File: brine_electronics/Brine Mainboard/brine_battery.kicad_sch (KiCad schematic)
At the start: 2 parts, among them J1 Conn_01x02_Socket

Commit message: Updated electronics/enclosure designs
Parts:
- BATT1: now left out of the parts list
- J1: footprint Connector_JST:JST_PH_B2B-PH-K_1x02_P2.00mm_Vertical -> Connector_JST:JST_PH_S2B-PH-K_1x02_P2.00mm_Horizontal
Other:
- moved on the sheet: BATT1
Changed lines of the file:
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@@
 	(wire
 		(pts
-			(xy 139.7 113.03) (xy 163.83 113.03)
-		)
-		(stroke
-			(width 0)
-			(type default)
-		)
-	)
-	(wire
-		(pts
-			(xy 139.7 115.57) (xy 163.83 115.57)
+			(xy 139.7 100.33) (xy 163.83 100.33)
+		)
+		(stroke
+			(width 0)
+			(type default)
+		)
+	)
+	(wire
+		(pts
+			(xy 139.7 102.87) (xy 163.83 102.87)
 		)
 		(stroke
@@
 	(hierarchical_label "BATT"
 		(shape output)
-		(at 163.83 113.03 0)
+		(at 163.83 100.33 0)
 		(effects
 			(font
@@
 	(symbol
 		(lib_id "power:GND")
-		(at 163.83 115.57 90)
+		(at 163.83 102.87 90)
 		(unit 1)
 		(exclude_from_sim no)
@@
 		(fields_autoplaced yes)
 		(property "Reference" "#PWR08"
-			(at 170.18 115.57 0)
+			(at 170.18 102.87 0)
 			(effects
 				(font
@@
 		)
 		(property "Value" "GND"
-			(at 167.64 115.5699 90)
+			(at 167.64 102.8699 90)
 			(effects
 				(font
@@
 		)
 		(property "Footprint" ""
-			(at 163.83 115.57 0)
+			(at 163.83 102.87 0)
 			(effects
 				(font
@@
 		)
 		(property "Datasheet" ""
-			(at 163.83 115.57 0)
+			(at 163.83 102.87 0)
 			(effects
 				(font
@@
 		)
 		(property "Description" "Power symbol creates a global label with name \"GND\" , ground"
-			(at 163.83 115.57 0)
+			(at 163.83 102.87 0)
 			(effects
 				(font
@@
 			)
 		)
-		(property "Footprint" "Connector_JST:JST_PH_B2B-PH-K_1x02_P2.00mm_Vertical"
+		(property "Footprint" "Connector_JST:JST_PH_S2B-PH-K_1x02_P2.00mm_Horizontal"
 			(at 134.62 90.17 0)
 			(effects
@@
 	(symbol
 		(lib_id "Connector:Conn_01x02_Pin")
-		(at 134.62 113.03 0)
-		(unit 1)
-		(exclude_from_sim no)
-		(in_bom yes)
+		(at 134.62 100.33 0)
+		(unit 1)
+		(exclude_from_sim no)
+		(in_bom no)
 		(on_board yes)
 		(dnp yes)
 		(property "Reference" "BATT1"
-			(at 130.556 114.3 0)
+			(at 130.556 101.6 0)
 			(effects
 				(font
@@
 		)
 		(property "Value" "Conn_01x02_Pin"
-			(at 135.255 110.49 0)
+			(at 135.255 97.79 0)
 			(effects
 				(font
@@
 		)
 		(property "Footprint" "Connector_PinHeader_2.54mm:PinHeader_1x02_P2.54mm_Vertical"
-			(at 134.62 113.03 0)
+			(at 134.62 100.33 0)
 			(effects
 				(font
@@
 		)
 		(property "Datasheet" "~"
-			(at 134.62 113.03 0)
+			(at 134.62 100.33 0)
 			(effects
 				(font
@@
 		)
 		(property "Description" "Generic connector, single row, 01x02, script generated"
-			(at 134.62 113.03 0)
-			(effects
-				(font
+			(at 134.62 100.33 0)
+			(effects
+				(font

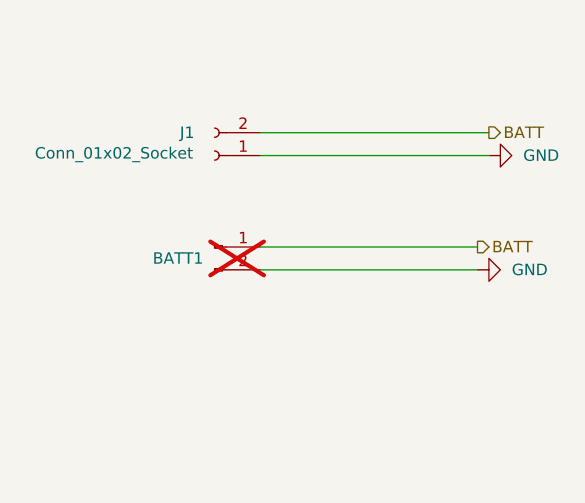
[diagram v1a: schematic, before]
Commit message: Implemented power latch circuit ⚡
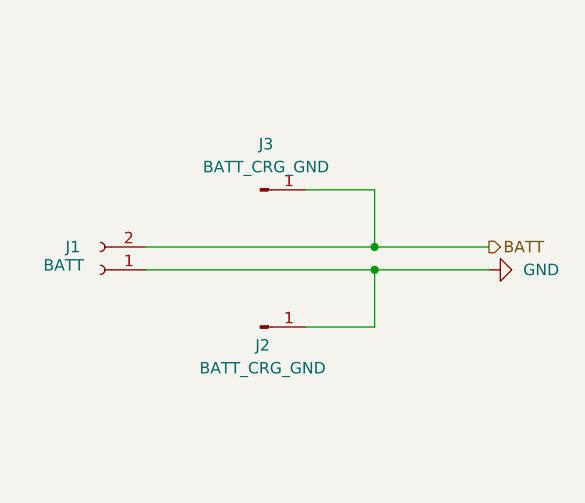
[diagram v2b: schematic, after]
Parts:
- removed BATT1: Conn_01x02_Pin, Connector_PinHeader_2.54mm:PinHeader_1x02_P2.54mm_Vertical, symbol Connector:Conn_01x02_Pin
- added J2, J3: BATT_CRG_GND, Connector_Wire:SolderWirePad_1x01_SMD_1.5x3mm, symbol Connector:Conn_01x01_Pin
- J1: value Conn_01x02_Socket -> BATT
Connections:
- net BATT: now also J3.1 (Pin_1)
- net GND: now also J2.1 (Pin_1)
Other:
- moved on the sheet: J1

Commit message: Resolved schematic DRC issues ✅
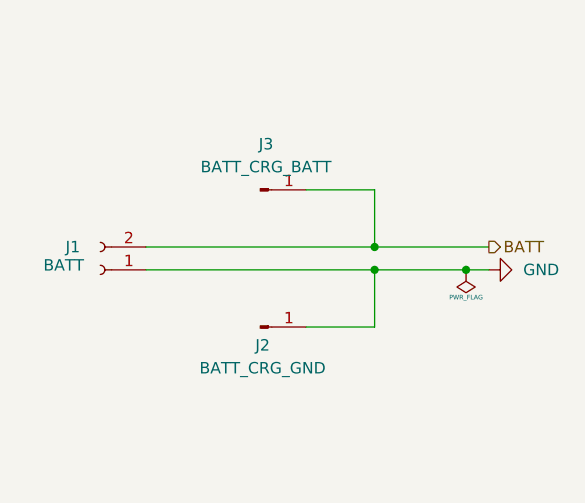
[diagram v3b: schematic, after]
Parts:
- J3: value BATT_CRG_GND -> BATT_CRG_BATT
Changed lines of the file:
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@@
 	(title_block
 		(title "Brine - Battery")
-		(date "2026-04-03")
+		(date "2026-04-07")
 		(rev "1.0.0")
 		(company "Splendid Endeavors")
@@
 		(color 0 0 0 0)
 	)
+	(junction
+		(at 162.56 102.87)
+		(diameter 0)
+		(color 0 0 0 0)
+	)
 	(wire
 		(pts
@@
 	(wire
 		(pts
-			(xy 152.4 102.87) (xy 165.1 102.87)
+			(xy 152.4 102.87) (xy 162.56 102.87)
 		)
 		(stroke
@@
 		(pts
 			(xy 144.78 93.98) (xy 152.4 93.98)
+		)
+		(stroke
+			(width 0)
+			(type default)
+		)
+	)
+	(wire
+		(pts
+			(xy 162.56 102.87) (xy 165.1 102.87)
 		)
 		(stroke
@@
 			)
 		)
-		(property "Value" "BATT_CRG_GND"
+		(property "Value" "BATT_CRG_BATT"
 			(at 140.335 91.44 0)
 			(effects
@@
 					(unit 1)
 				)
+			)
+		)
+	)
+	(symbol
+		(lib_id "power:PWR_FLAG")
+		(at 162.56 102.87 180)
+		(unit 1)
+		(exclude_from_sim no)
+		(in_bom yes)
+		(on_board yes)
+		(dnp no)
+		(property "Reference" "#FLG03"
+			(at 162.56 104.775 0)
+			(effects
+				(font
+					(size 1.27 1.27)
+				)
+				(hide yes)
+			)
+		)
+		(property "Value" "PWR_FLAG"
+			(at 162.56 105.918 0)
+			(effects
+				(font
+					(size 0.508 0.508)
+				)
+			)
+		)
+		(property "Footprint" ""
+			(at 162.56 102.87 0)
+			(effects
+				(font
+					(size 1.27 1.27)
+				)
+				(hide yes)
+			)
+		)
+		(property "Datasheet" "~"
+			(at 162.56 102.87 0)
+			(effects
+				(font
+					(size 1.27 1.27)
+				)
+				(hide yes)
+			)
+		)
+		(property "Description" "Special symbol for telling ERC where power comes from"
+			(at 162.56 102.87 0)
+			(effects
+				(font
+					(size 1.27 1.27)
+				)
+				(hide yes)
+			)
+		)
+		(pin "1"
+		)
+		(instances
+			(project ""
+				(path "/da3a4ef2-0e38-46f1-a1fc-55d8e0a83a54/cb6fa39a-9a0c-434c-b5c9-65b8cf34a8e9"
+					(reference "#FLG03")
+					(unit 1)
+				)

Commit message: Updated lower latch circuit ⚡
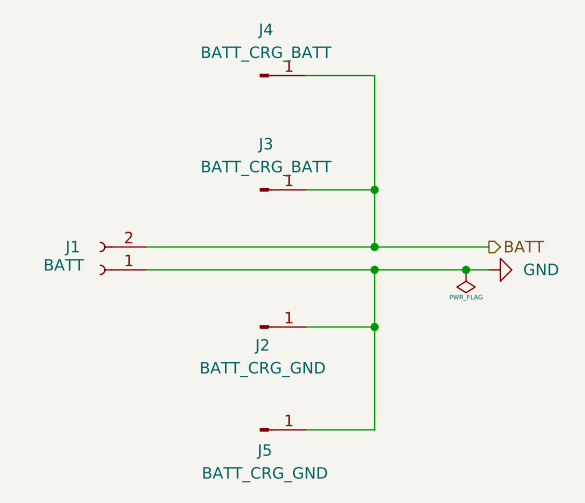
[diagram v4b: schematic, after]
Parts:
- added J4: BATT_CRG_BATT, Connector_PinHeader_1.00mm:PinHeader_1x01_P1.00mm_Vertical, symbol Connector:Conn_01x01_Pin
- added J5: BATT_CRG_GND, Connector_PinHeader_1.00mm:PinHeader_1x01_P1.00mm_Vertical, symbol Connector:Conn_01x01_Pin
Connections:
- net BATT: now also J4.1 (Pin_1)
- net GND: now also J5.1 (Pin_1)

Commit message: Updated production files 🏭
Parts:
- J1, J2, J3, J4, J5: now left out of the parts list
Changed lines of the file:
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@@
 		(body_style 1)
 		(exclude_from_sim no)
-		(in_bom yes)
+		(in_bom no)
 		(on_board yes)
 		(in_pos_files yes)
@@
 		)
 		(property "Description" "Generic connector, single row, 01x02, script generated"
+			(at 121.92 102.87 0)
+			(hide yes)
+			(show_name no)
+			(do_not_autoplace no)
+			(effects
+				(font
+					(size 1.27 1.27)
+				)
+			)
+		)
+		(property "Color" ""
+			(at 121.92 102.87 0)
+			(hide yes)
+			(show_name no)
+			(do_not_autoplace no)
+			(effects
+				(font
+					(size 1.27 1.27)
+				)
+			)
+		)
+		(property "LCSC Part #" ""
 			(at 121.92 102.87 0)
 			(hide yes)
@@
 		(body_style 1)
 		(exclude_from_sim no)
-		(in_bom yes)
+		(in_bom no)
 		(on_board yes)
 		(in_pos_files yes)
@@
 		)
 		(property "Description" "Generic connector, single row, 01x01, script generated"
+			(at 139.7 120.65 0)
+			(hide yes)
+			(show_name no)
+			(do_not_autoplace no)
+			(effects
+				(font
+					(size 1.27 1.27)
+				)
+			)
+		)
+		(property "Color" ""
+			(at 139.7 120.65 0)
+			(hide yes)
+			(show_name no)
+			(do_not_autoplace no)
+			(effects
+				(font
+					(size 1.27 1.27)
+				)
+			)
+		)
+		(property "LCSC Part #" ""
 			(at 139.7 120.65 0)
 			(hide yes)
@@
 		(body_style 1)
 		(exclude_from_sim no)
-		(in_bom yes)
+		(in_bom no)
 		(on_board yes)
 		(in_pos_files yes)
@@
 		)
 		(property "Description" "Generic connector, single row, 01x01, script generated"
+			(at 139.7 93.98 0)
+			(hide yes)
+			(show_name no)
+			(do_not_autoplace no)
+			(effects
+				(font
+					(size 1.27 1.27)
+				)
+			)
+		)
+		(property "Color" ""
+			(at 139.7 93.98 0)
+			(hide yes)
+			(show_name no)
+			(do_not_autoplace no)
+			(effects
+				(font
+					(size 1.27 1.27)
+				)
+			)
+		)
+		(property "LCSC Part #" ""
 			(at 139.7 93.98 0)
 			(hide yes)
@@
 		(body_style 1)
 		(exclude_from_sim no)
-		(in_bom yes)
+		(in_bom no)
 		(on_board yes)
 		(in_pos_files yes)
@@
 		)
 		(property "Description" "Generic connector, single row, 01x01, script generated"
+			(at 139.7 109.22 0)
+			(hide yes)
+			(show_name no)
+			(do_not_autoplace no)
+			(effects
+				(font
+					(size 1.27 1.27)
+				)
+			)
+		)
+		(property "Color" ""
+			(at 139.7 109.22 0)
+			(hide yes)
+			(show_name no)
+			(do_not_autoplace no)
+			(effects
+				(font
+					(size 1.27 1.27)
+				)
+			)
+		)
+		(property "LCSC Part #" ""
 			(at 139.7 109.22 0)
 			(hide yes)
@@
 		(body_style 1)
 		(exclude_from_sim no)
-		(in_bom yes)
+		(in_bom no)
 		(on_board yes)
 		(in_pos_files yes)
@@
 			(at 139.7 81.28 0)
 			(hide yes)
+			(show_name no)
+			(do_not_autoplace no)
+			(effects
+				(font
+					(size 1.27 1.27)
+				)
+			)
+		)
+		(property "Color" ""
+			(at 139.7 81.28 0)
+			(hide yes)
+			(show_name no)
+			(do_not_autoplace no)
+			(effects
+				(font
+					(size 1.27 1.27)
+				)
+			)
+		)
+		(property "LCSC Part #" ""
+			(at 139.7 81.28 0)
+			(hide yes)
